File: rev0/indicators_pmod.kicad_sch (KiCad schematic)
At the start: 32 parts, among them IC1 ECP5-BGA256, U14 74AUP2G126, U2 74AUP2G126

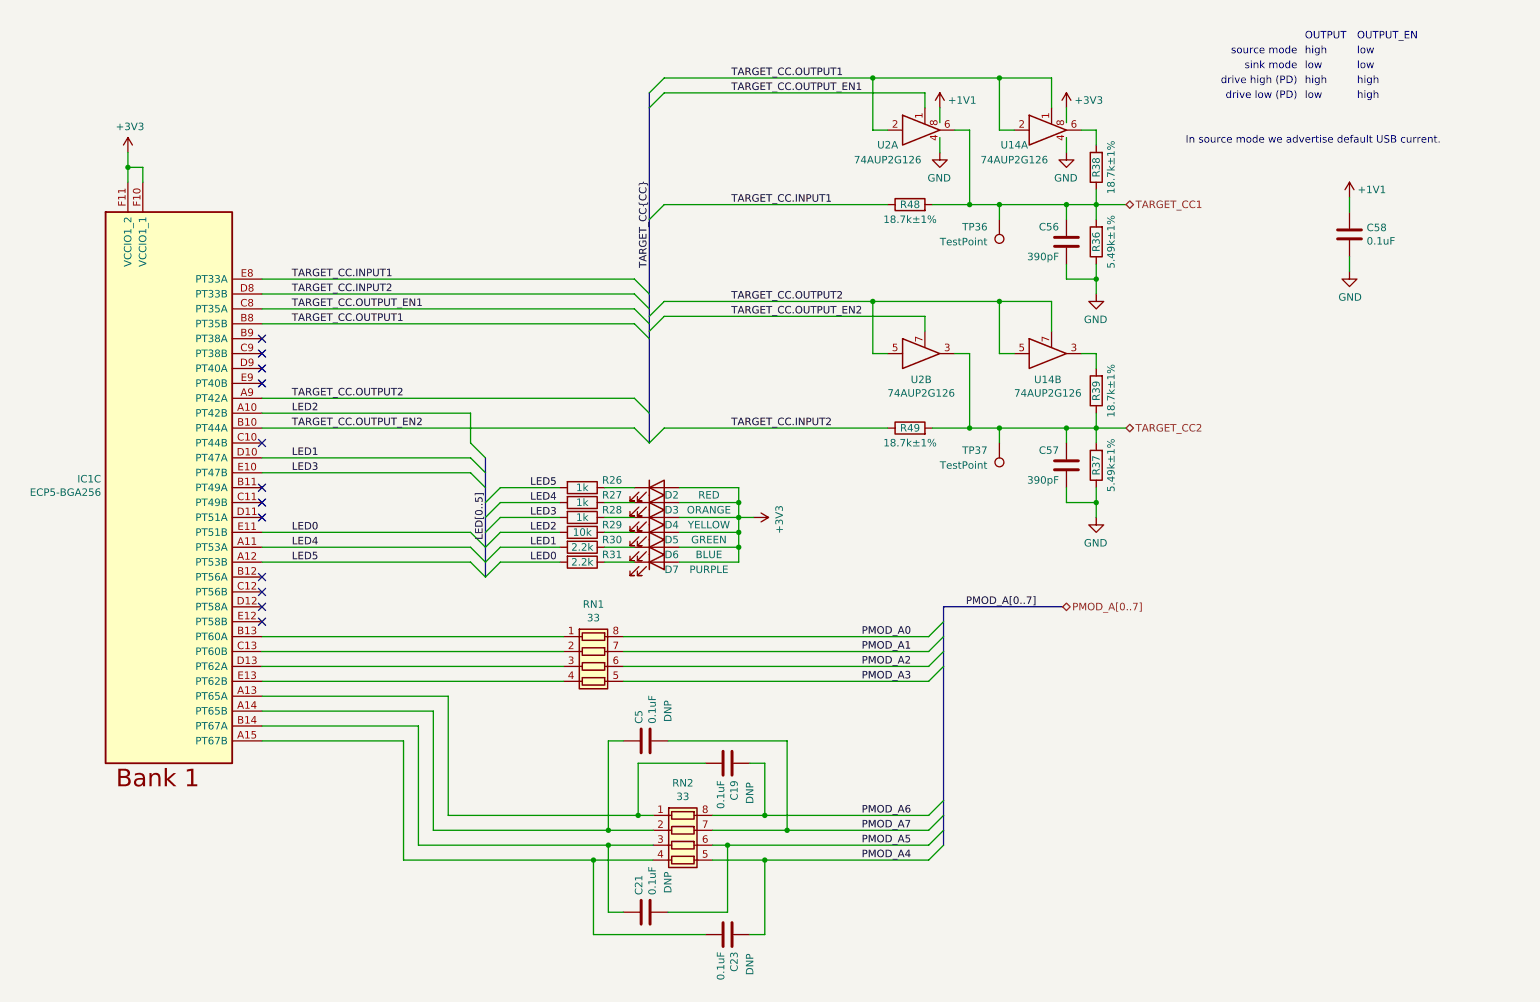
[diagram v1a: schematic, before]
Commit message: hardware: add Target port Type-C controller
replaces buffers for CC pin I/O
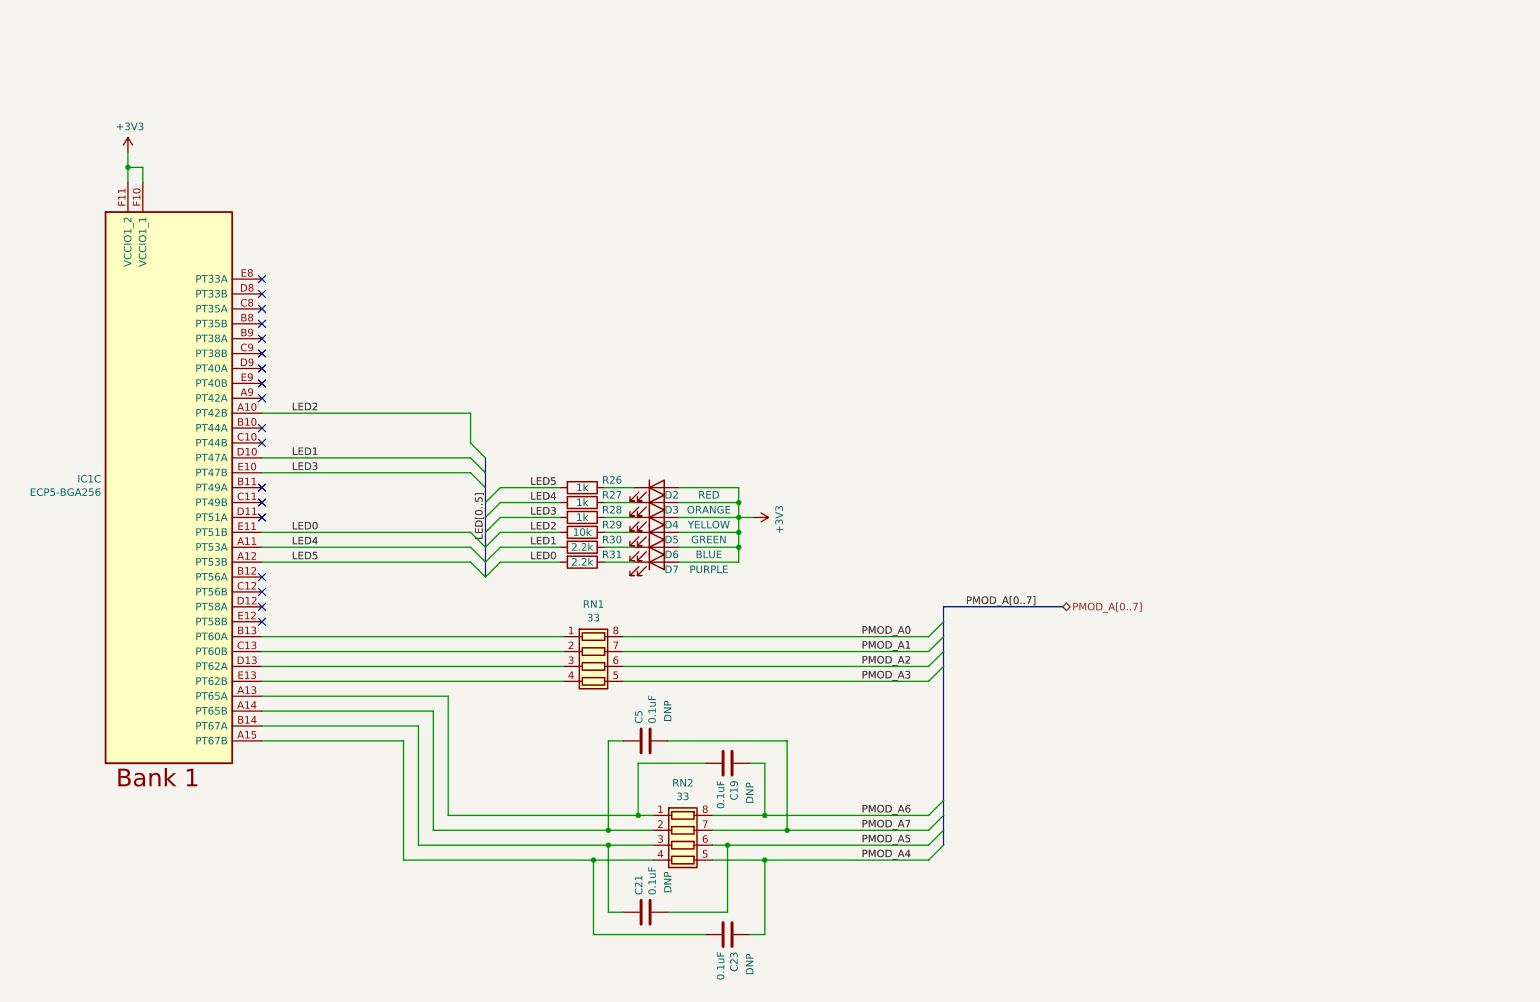
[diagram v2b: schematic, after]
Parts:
- removed C56, C57: 390pF, Capacitor_SMD:C_0402_1005Metric, symbol Device:C
- removed C58: 0.1uF, Capacitor_SMD:C_0402_1005Metric, symbol Device:C
- removed R36, R37: 5.49k±1%, Resistor_SMD:R_0402_1005Metric, symbol Device:R
- removed R38, R39, R48, R49: 18.7k±1%, Resistor_SMD:R_0402_1005Metric, symbol Device:R
- removed TP36, TP37: TestPoint, TestPoint:TestPoint_Pad_D1.0mm, symbol Connector:TestPoint
- removed U14, U2: 74AUP2G126, luna:X2-DFN1210-8_1.2x1mm_P0.3mm, symbol support_hardware:74AUP2G126
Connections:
- net TARGET_CC.INPUT1: no longer names the net of IC1.E8 (PT33A)
- net TARGET_CC.INPUT2: no longer names the net of IC1.D8 (PT33B)
- net TARGET_CC.OUTPUT1: no longer names the net of IC1.B8 (PT35B)
- net TARGET_CC.OUTPUT2: no longer names the net of IC1.A9 (PT42A)
- net TARGET_CC.OUTPUT_EN1: no longer names the net of IC1.C8 (PT35A)
- net TARGET_CC.OUTPUT_EN2: no longer names the net of IC1.B10 (PT44A)
- no-connect marks 12 -> 18
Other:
- note removed: "In source mode we advertise default USB current."
- note removed: "OUTPUT"
- note removed: "OUTPUT_EN"
- note removed: "drive high (PD)"
- note removed: "drive low (PD)"
- note removed: "high"
- note removed: "low"
- note removed: "sink mode"
- note removed: "source mode"

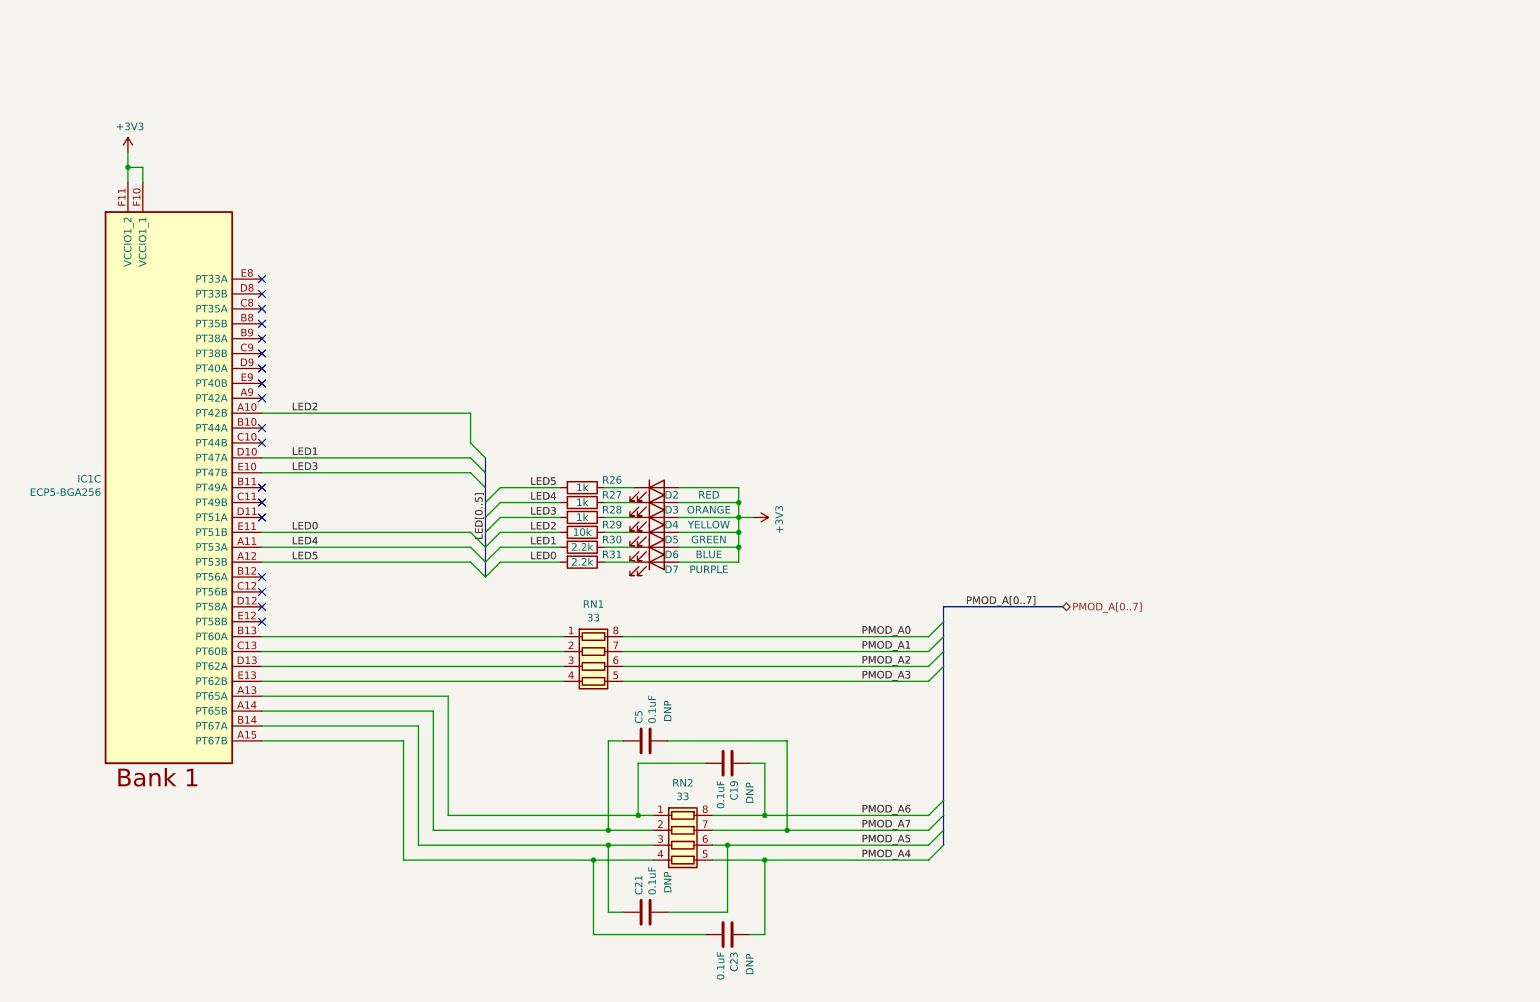
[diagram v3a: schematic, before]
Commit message: hardware: update layout to match schematic
- invert USB switch D+/D- for routing convenience
- connect *_VBUS_CLAMPED to *_VBUS_IN not *_VBUS
- reassign FPGA pins and banks for routing convenience
- connect PHY VBAT to +3V3, not +5V
- add PHY VDD33 test points
- add LED test points
- add PROGRAM button test point
- add PHY VDD33 test point
- add mezzanine connector
- improve decoupling
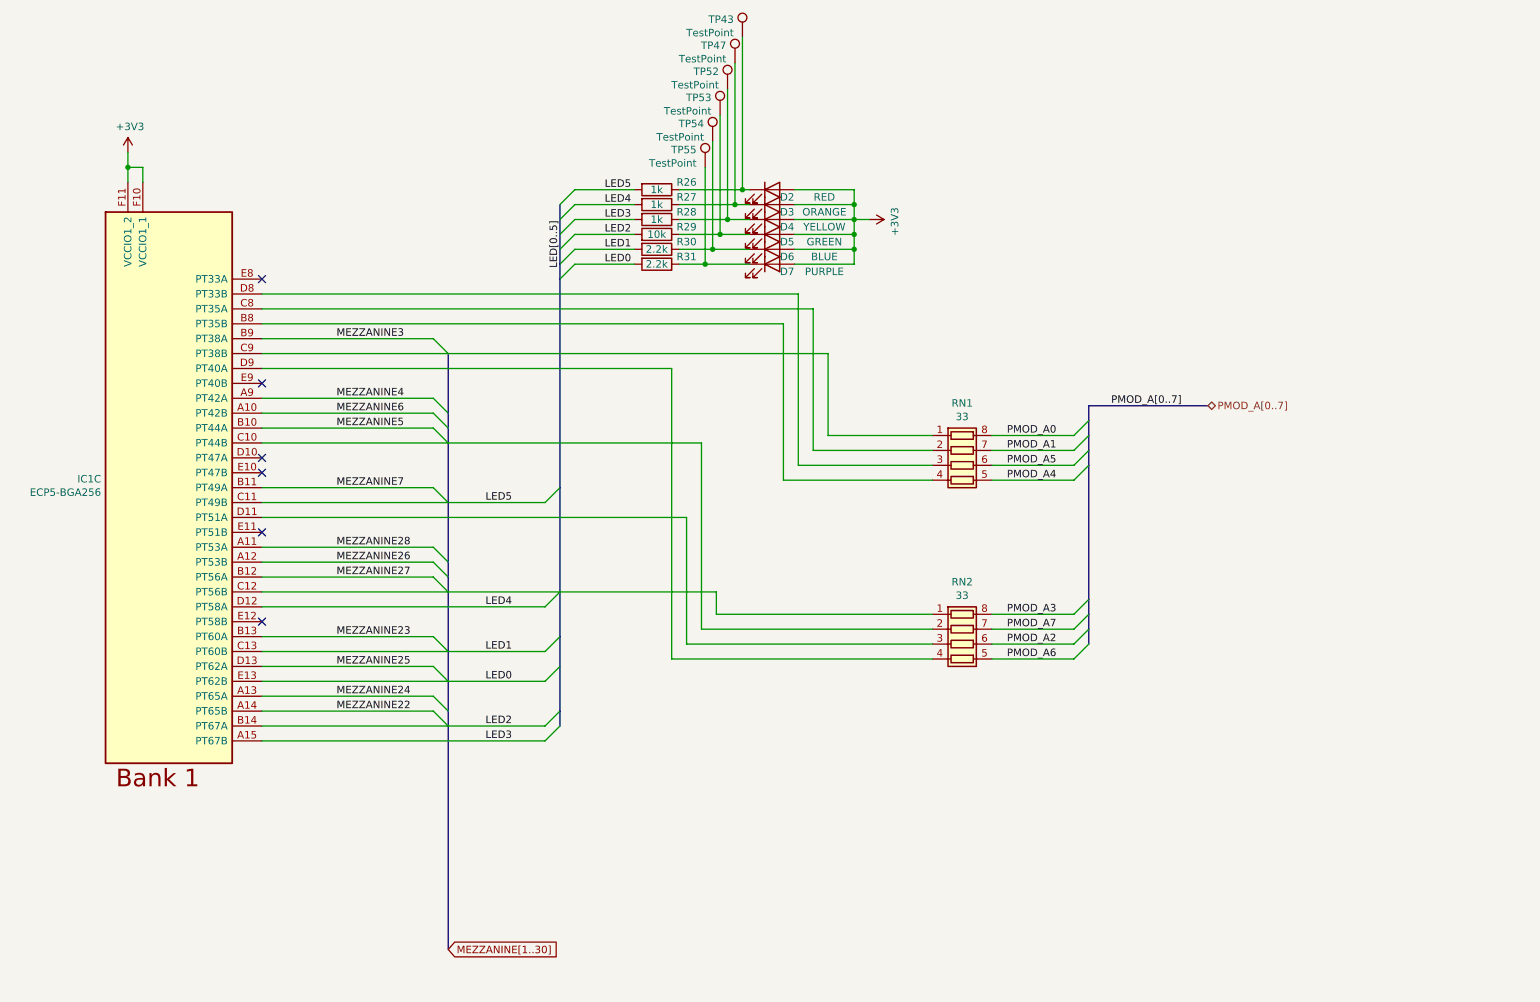
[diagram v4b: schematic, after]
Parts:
- removed C19, C21, C23, C5: 0.1uF, Capacitor_SMD:C_0402_1005Metric, symbol Device:C
- added TP43, TP47, TP52, TP53, TP54, TP55: TestPoint, TestPoint:TestPoint_Pad_D1.0mm, symbol Connector:TestPoint
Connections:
- net LED0: now also IC1.E13 (PT62B); no longer IC1.E11 (PT51B)
- net LED1: now also IC1.C13 (PT60B); no longer IC1.D10 (PT47A)
- net LED2: now also IC1.B14 (PT67A); no longer IC1.A10 (PT42B)
- net LED3: now also IC1.A15 (PT67B); no longer IC1.E10 (PT47B)
- net LED4: now also IC1.D12 (PT58A); no longer IC1.A11 (PT53A)
- net LED5: now also IC1.C11 (PT49B); no longer IC1.A12 (PT53B)
- net PMOD_A2: now also RN2.6 (R3.2); no longer RN1.6 (R3.2)
- net PMOD_A3: now also RN2.8 (R1.2); no longer RN1.5 (R4.2)
- net PMOD_A4: now also RN1.5 (R4.2); no longer RN2.5 (R4.2)
- net PMOD_A5: now also RN1.6 (R3.2); no longer RN2.6 (R3.2)
- net PMOD_A6: now also RN2.5 (R4.2); no longer RN2.8 (R1.2)
- net at D5.1 (K), R29.1: now also TP53.1
- net at D6.1 (K), R30.1: now also TP54.1
- net at D7.1 (K), R31.1: now also TP55.1
- net at D2.1 (K), R26.1: now also TP43.1
- net at D3.1 (K), R27.1: now also TP47.1
- net at D4.1 (K), R28.1: now also TP52.1
- net at RN2.1 (R1.1): now also IC1.C12 (PT56B); no longer IC1.A13 (PT65A)
- net at RN2.2 (R2.1): now also IC1.C10 (PT44B); no longer IC1.A14 (PT65B)
- net at RN2.4 (R4.1): now also IC1.D9 (PT40A); no longer IC1.A15 (PT67B)
- net MEZZANINE4: now reaches IC1.A9 (PT42A)
- net MEZZANINE5: now reaches IC1.B10 (PT44A)
- net MEZZANINE7: now reaches IC1.B11 (PT49A)
- net MEZZANINE27: now reaches IC1.B12 (PT56A)
- net at RN1.1 (R1.1): now also IC1.C9 (PT38B); no longer IC1.B13 (PT60A)
- net at RN2.3 (R3.1): now also IC1.D11 (PT51A); no longer IC1.B14 (PT67A)
- net at IC1.B8 (PT35B): now also RN1.4 (R4.1)
- net MEZZANINE3: now reaches IC1.B9 (PT38A)
- net at RN1.2 (R2.1): now also IC1.C8 (PT35A); no longer IC1.C13 (PT60B)
- net at RN1.3 (R3.1): now also IC1.D8 (PT33B); no longer IC1.D13 (PT62A)
- new net MEZZANINE22: IC1.A14 (PT65B)
- new net MEZZANINE23: IC1.B13 (PT60A)
- new net MEZZANINE24: IC1.A13 (PT65A)
- new net MEZZANINE25: IC1.D13 (PT62A)
- new net MEZZANINE26: IC1.A12 (PT53B)
- new net MEZZANINE28: IC1.A11 (PT53A)
- new net MEZZANINE6: IC1.A10 (PT42B)
- no-connect marks 18 -> 6
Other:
- moved on the sheet: D2, D3, D4, D5, D6, D7, R26, R27, R28, R29, R30, R31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

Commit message: hardware: passive component selection
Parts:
- R26, R27, R28: Manufacturer (none) -> Yageo; Part Number GENERIC-RES-0402-1K -> RC0402JR-071KL
- R29: Manufacturer (none) -> Yageo; Part Number GENERIC-RES-0402-10K -> RC0402JR-0710KL
- R30, R31: Manufacturer (none) -> Yageo; Part Number GENERIC-RES-0402-2.2K -> RC0402JR-072K2L
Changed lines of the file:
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@@
       (effects (font (size 1.27 1.27)) hide)
     )
-    (property "Part Number" "GENERIC-RES-0402-10K" (id 4) (at 143.51 55.88 0)
+    (property "Part Number" "RC0402JR-0710KL" (id 4) (at 143.51 55.88 0)
       (effects (font (size 1.27 1.27)) hide)
     )
     (property "Substitution" "any equivalent" (id 5) (at 143.51 55.88 0)
+      (effects (font (size 1.27 1.27)) hide)
+    )
+    (property "Description" "RES 10K OHM 5% 1/16W 0402" (id 6) (at 143.51 55.88 0)
+      (effects (font (size 1.27 1.27)) hide)
+    )
+    (property "Manufacturer" "Yageo" (id 7) (at 143.51 55.88 0)
       (effects (font (size 1.27 1.27)) hide)
     )
@@
       (effects (font (size 1.27 1.27)) hide)
     )
-    (property "Part Number" "GENERIC-RES-0402-2.2K" (id 4) (at 143.51 58.42 0)
+    (property "Part Number" "RC0402JR-072K2L" (id 4) (at 143.51 58.42 0)
       (effects (font (size 1.27 1.27)) hide)
     )
     (property "Substitution" "any equivalent" (id 5) (at 143.51 58.42 0)
+      (effects (font (size 1.27 1.27)) hide)
+    )
+    (property "Description" "RES 2.2K OHM 5% 1/16W 0402" (id 6) (at 143.51 58.42 0)
+      (effects (font (size 1.27 1.27)) hide)
+    )
+    (property "Manufacturer" "Yageo" (id 7) (at 143.51 58.42 0)
       (effects (font (size 1.27 1.27)) hide)
     )
@@
       (effects (font (size 1.27 1.27)) hide)
     )
-    (property "Part Number" "GENERIC-RES-0402-2.2K" (id 4) (at 143.51 60.96 0)
+    (property "Part Number" "RC0402JR-072K2L" (id 4) (at 143.51 60.96 0)
       (effects (font (size 1.27 1.27)) hide)
     )
     (property "Substitution" "any equivalent" (id 5) (at 143.51 60.96 0)
+      (effects (font (size 1.27 1.27)) hide)
+    )
+    (property "Description" "RES 2.2K OHM 5% 1/16W 0402" (id 6) (at 143.51 60.96 0)
+      (effects (font (size 1.27 1.27)) hide)
+    )
+    (property "Manufacturer" "Yageo" (id 7) (at 143.51 60.96 0)
       (effects (font (size 1.27 1.27)) hide)
     )
@@
       (effects (font (size 1.27 1.27)) hide)
     )
-    (property "Part Number" "GENERIC-RES-0402-1K" (id 4) (at 143.51 48.26 0)
+    (property "Part Number" "RC0402JR-071KL" (id 4) (at 143.51 48.26 0)
       (effects (font (size 1.27 1.27)) hide)
     )
     (property "Substitution" "any equivalent" (id 5) (at 143.51 48.26 0)
+      (effects (font (size 1.27 1.27)) hide)
+    )
+    (property "Description" "RES 1K OHM 5% 1/16W 0402" (id 6) (at 143.51 48.26 0)
+      (effects (font (size 1.27 1.27)) hide)
+    )
+    (property "Manufacturer" "Yageo" (id 7) (at 143.51 48.26 0)
       (effects (font (size 1.27 1.27)) hide)
     )
@@
       (effects (font (size 1.27 1.27)) hide)
     )
-    (property "Part Number" "GENERIC-RES-0402-1K" (id 4) (at 143.51 50.8 0)
+    (property "Part Number" "RC0402JR-071KL" (id 4) (at 143.51 50.8 0)
       (effects (font (size 1.27 1.27)) hide)
     )
     (property "Substitution" "any equivalent" (id 5) (at 143.51 50.8 0)
+      (effects (font (size 1.27 1.27)) hide)
+    )
+    (property "Description" "RES 1K OHM 5% 1/16W 0402" (id 6) (at 143.51 50.8 0)
+      (effects (font (size 1.27 1.27)) hide)
+    )
+    (property "Manufacturer" "Yageo" (id 7) (at 143.51 50.8 0)
       (effects (font (size 1.27 1.27)) hide)
     )
@@
       (effects (font (size 1.27 1.27)) hide)
     )
-    (property "Part Number" "GENERIC-RES-0402-1K" (id 4) (at 143.51 53.34 0)
+    (property "Part Number" "RC0402JR-071KL" (id 4) (at 143.51 53.34 0)
       (effects (font (size 1.27 1.27)) hide)
     )
@@
       (effects (font (size 1.27 1.27)) hide)
     )
+    (property "Description" "RES 1K OHM 5% 1/16W 0402" (id 6) (at 143.51 53.34 0)
+      (effects (font (size 1.27 1.27)) hide)
+    )
+    (property "Manufacturer" "Yageo" (id 7) (at 143.51 53.34 0)
+      (effects (font (size 1.27 1.27)) hide)
+    )
